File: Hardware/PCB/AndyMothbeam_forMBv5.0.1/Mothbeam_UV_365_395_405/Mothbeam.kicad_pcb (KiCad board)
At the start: 2 copper layers, 27.8 x 45 mm, 23 parts, among them CN1 X6511FRS-04-C85D30, SW2 SW_DIP_x04, U1 BCR421U, U2 BCR421U, U3 BCR421U

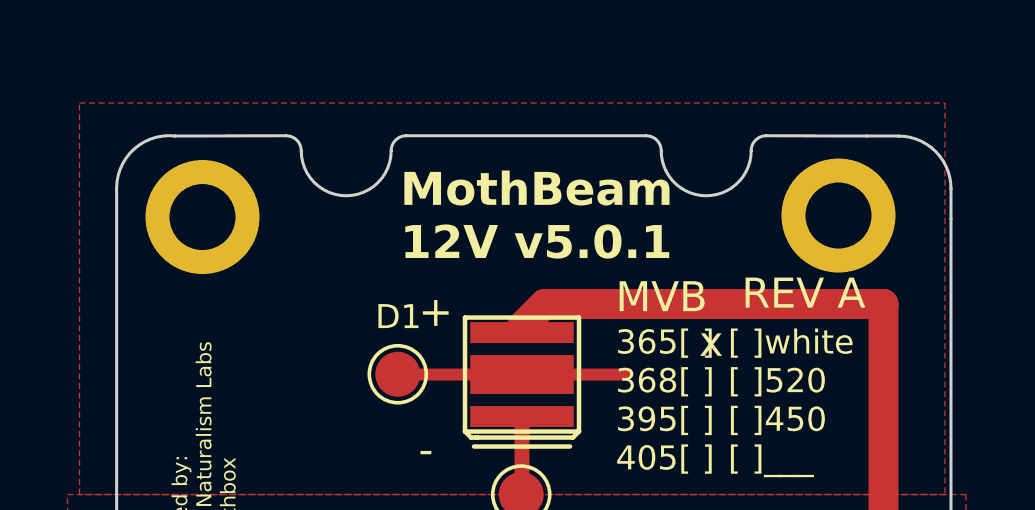
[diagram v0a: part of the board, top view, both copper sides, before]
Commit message: MADE UV m3 holes ready for JLCPCB
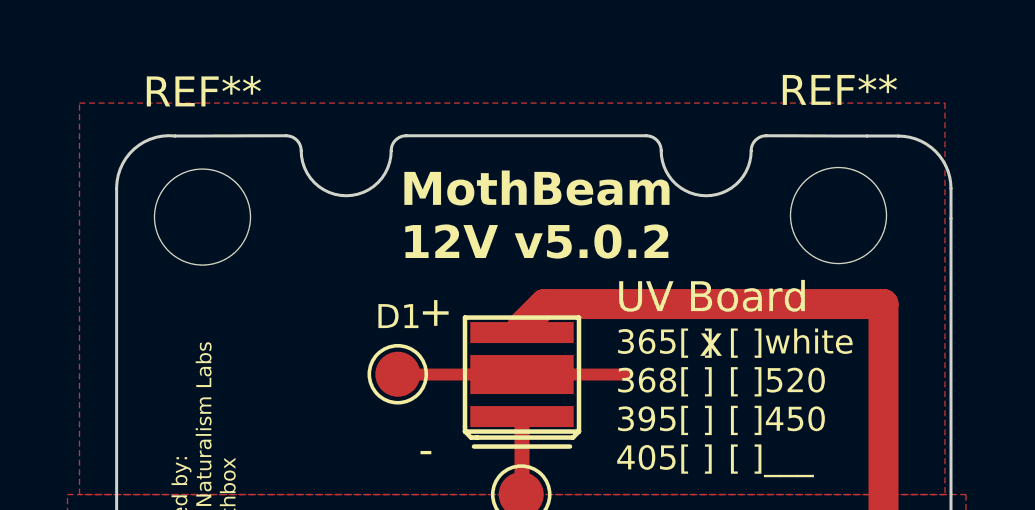
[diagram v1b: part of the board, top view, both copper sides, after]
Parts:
- REF** (x2): value MountingHole_2.2mm_M2_DIN965_Pad -> MountingHole_3.2mm_M3; footprint MountingHole:MountingHole_2.2mm_M2_DIN965_Pad -> MountingHole:MountingHole_3.2mm_M3
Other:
- board text added: "MothBeam 12V v5.0.2"
- board text added: "UV Board"
- board text removed: "MVB"
- board text removed: "MothBeam 12V v5.0.1"
- board text removed: "REV A"
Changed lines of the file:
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@@
 	(net 16 "Net-(D1--)")
 	(net 17 "Net-(D2-A)")
-	(footprint "MountingHole:MountingHole_2.2mm_M2_DIN965_Pad"
+	(footprint "MountingHole:MountingHole_3.2mm_M3"
 		(layer "F.Cu")
 		(at 102.1 32.7)
-		(descr "Mounting Hole 2.2mm, M2, generated by kicad-footprint-generator mountinghole.py")
-		(tags "mountinghole M2 DIN965")
+		(descr "Mounting Hole 3.2mm, M3, no annular, generated by kicad-footprint-generator mountinghole.py")
+		(tags "mountinghole M3")
 		(property "Reference" "REF**"
-			(at 0 -2.85 0)
+			(at 0 -4.15 0)
 			(layer "F.SilkS")
-			(hide yes)
 			(effects
 				(font
-					(size 0.8 0.8)
+					(size 1 1)
 					(thickness 0.15)
 				)
 			)
 		)
-		(property "Value" "MountingHole_2.2mm_M2_DIN965_Pad"
-			(at 0 2.85 0)
+		(property "Value" "MountingHole_3.2mm_M3"
+			(at 0 4.15 0)
 			(layer "F.Fab")
 			(effects
@@
 		(fp_circle
 			(center 0 0)
-			(end 1.9 0)
+			(end 3.2 0)
 			(stroke
 				(width 0.15)
@@
 		(fp_circle
 			(center 0 0)
-			(end 2.15 0)
+			(end 3.45 0)
 			(stroke
 				(width 0.05)
@@
 			(effects
 				(font
-					(size 0.95 0.95)
-					(thickness 0.14)
+					(size 1 1)
+					(thickness 0.15)
 				)
 			)
 		)
-		(pad "1" thru_hole circle
+		(pad "" np_thru_hole circle
 			(at 0 0)
-			(size 3.8 3.8)
-			(drill 2.2)
+			(size 3.2 3.2)
+			(drill 3.2)
 			(layers "*.Cu" "*.Mask")
-			(remove_unused_layers no)
-			(zone_connect 2)
 		)
 		(embedded_fonts no)
@@
 		)
 	)
-	(footprint "MountingHole:MountingHole_2.2mm_M2_DIN965_Pad"
+	(footprint "MountingHole:MountingHole_3.2mm_M3"
 		(layer "F.Cu")
 		(at 123.3 32.65)
-		(descr "Mounting Hole 2.2mm, M2, generated by kicad-footprint-generator mountinghole.py")
-		(tags "mountinghole M2 DIN965")
+		(descr "Mounting Hole 3.2mm, M3, no annular, generated by kicad-footprint-generator mountinghole.py")
+		(tags "mountinghole M3")
 		(property "Reference" "REF**"
-			(at 0 -2.85 0)
+			(at 0 -4.15 0)
 			(layer "F.SilkS")
-			(hide yes)
 			(effects
 				(font
-					(size 0.8 0.8)
+					(size 1 1)
 					(thickness 0.15)
 				)
 			)
 		)
-		(property "Value" "MountingHole_2.2mm_M2_DIN965_Pad"
-			(at 0 2.85 0)
+		(property "Value" "MountingHole_3.2mm_M3"
+			(at 0 4.15 0)
 			(layer "F.Fab")
 			(effects
@@
 		(fp_circle
 			(center 0 0)
-			(end 1.9 0)
+			(end 3.2 0)
 			(stroke
 				(width 0.15)
@@
 		(fp_circle
 			(center 0 0)
-			(end 2.15 0)
+			(end 3.45 0)
 			(stroke
 				(width 0.05)
@@
 			(effects
 				(font
-					(size 0.95 0.95)
-					(thickness 0.14)
+					(size 1 1)
+					(thickness 0.15)
 				)
 			)
 		)
-		(pad "1" thru_hole circle
+		(pad "" np_thru_hole circle
 			(at 0 0)
-			(size 3.8 3.8)
-			(drill 2.2)
+			(size 3.2 3.2)
+			(drill 3.2)
 			(layers "*.Cu" "*.Mask")
-			(remove_unused_layers no)
-			(zone_connect 2)
 		)
 		(embedded_fonts no)
@@
 		)
 	)
-	(gr_text "REV A"
-		(at 120.07 35.84 0)
-		(layer "F.SilkS")
-		(effects
-			(font
-				(size 1 1)
-				(thickness 0.15)
-			)
-			(justify left bottom)
-		)
-	)
 	(gr_text "x"
 		(at 118.55 55.6 0)
@@
 		)
 	)
-	(gr_text "MothBeam\n12V v5.0.1"
+	(gr_text "MothBeam\n12V v5.0.2"
 		(at 108.69 34.2 0)
 		(layer "F.SilkS" knockout)
@@
 			(justify left bottom)
 		)
-		(render_cache "MothBeam\n12V v5.0.1" 0
+		(render_cache "MothBeam\n12V v5.0.2" 0
 			(polygon
 				(pts
@@
 			(polygon
 				(pts
-					(xy 115.999693 34.013) (xy 115.767162 34.013) (xy 115.767162 33.376997) (xy 115.768707 33.27309)
-					(xy 115.773341 33.158302) (xy 115.740228 33.191415) (xy 115.693278 33.23373) (xy 115.566938 33.335421)
-					(xy 115.454568 33.195244) (xy 115.808738 32.913412) (xy 115.999693 32.913412)
+					(xy 116.193738 34.013) (xy 115.425283 34.013) (xy 115.425283 33.851329) (xy 115.700935 33.572587)
+					(xy 115.834933 33.428581) (xy 115.880699 33.370849) (xy 115.908817 33.323868) (xy 115.926106 33.27531)
+					(xy 115.931922 33.222984) (xy 115.927386 33.180351) (xy 115.915048 33.148366) (xy 115.895719 33.12445)
+					(xy 115.86987 33.106988) (xy 115.837855 33.096013) (xy 115.797991 33.092076) (xy 115.736043 33.099294)
+					(xy 115.67474 33.12136) (xy 115.615191 33.155418) (xy 115.548467 33.204513) (xy 115.422193 33.055134)
+					(xy 115.522272 32.9789) (xy 115.579286 32.946623) (xy 115.646262 32.920397) (xy 115.720273 32.904058)
+					(xy 115.814918 32.898031) (xy 115.885918 32.902734) (xy 115.947282 32.916089) (xy 116.000499 32.937323)
+					(xy 116.049213 32.967155) (xy 116.088909 33.002481) (xy 116.120594 33.043581) (xy 116.143986 33.089802)
+					(xy 116.158135 33.14002) (xy 116.162976 33.195244) (xy 116.15883 33.254988) (xy 116.146699 33.310199)
+					(xy 116.126773 33.361616) (xy 116.083716 33.434901) (xy 116.021993 33.510995) (xy 115.949161 33.585977)
+					(xy 115.856494 33.67421) (xy 115.714839 33.806663) (xy 115.714839 33.81741) (xy 116.193738 33.81741)
 				)
 			)
 		)
 	)
-	(gr_text "MVB"
+	(gr_text "UV Board"
 		(at 115.87 35.96 0)
 		(layer "F.SilkS")
@@
 	)
 	(zone
+		(net 9)
+		(net_name "/T2")
+		(layer "F.Cu")
+		(hatch edge 0.5)
+		(connect_pads
+			(clearance 0.35)
+		)
+		(min_thickness 0.25)
+		(filled_areas_thickness no)
+		(fill yes
+			(thermal_gap 0.5)
+			(thermal_bridge_width 0.5)
+			(smoothing chamfer)
+		)
+		(polygon
+			(pts
+				(xy 127.55 41.95) (xy 127.55 49.95) (xy 97.6 49.95) (xy 97.6 41.95)
+			)
+		)
+	)
+	(zone
 		(net 16)
 		(net_name "Net-(D1--)")
@@
 		(name "$teardrop_padvia$")
 		(hatch none 0.1)
-		(priority 30000)
+		(priority 30003)
 		(attr
 			(teardrop
@@
 		(polygon
 			(pts
-				(xy 112.2246 43.435589) (xy 113.2246 43.435589) (xy 113.460189 42.096318) (xy 112.7246 41.949) (xy 111.989011 42.096318)
-			)
-		)
-	)
-	(zone
-		(net 9)
-		(net_name "/T2")
-		(layer "F.Cu")
-		(hatch edge 0.5)
-		(connect_pads
-			(clearance 0.35)
-		)
-		(min_thickness 0.25)
-		(filled_areas_thickness no)
-		(fill yes
-			(thermal_gap 0.5)
-			(thermal_bridge_width 0.5)
-			(smoothing chamfer)
-		)
-		(polygon
-			(pts
-				(xy 127.55 41.95) (xy 127.55 49.95) (xy 97.6 49.95) (xy 97.6 41.95)
+				(xy 113 40.464411) (xy 112.5 40.464411) (xy 111.989011 41.803682) (xy 112.7246 41.951) (xy 113.460189 41.803682)
 			)
 		)
@@
 		(name "$teardrop_padvia$")
 		(hatch none 0.1)
-		(priority 30002)
+		(priority 30001)
 		(attr
 			(teardrop
@@
 		(polygon
 			(pts
-				(xy 112.25 51.435589) (xy 113.25 51.435589) (xy 113.485589 50.096318) (xy 112.75 49.949) (xy 112.014411 50.096318)
+				(xy 113.25 48.464411) (xy 112.25 48.464411) (xy 112.014411 49.803682) (xy 112.75 49.951) (xy 113.485589 49.803682)
 			)
 		)
 	)
 	(zone
-		(net 16)
-		(net_name "Net-(D1--)")
+		(net 17)
+		(net_name "Net-(D2-A)")
 		(layer "F.Cu")
 		(name "$teardrop_padvia$")
 		(hatch none 0.1)
-		(priority 30003)
+		(priority 30002)
 		(attr
 			(teardrop
@@
 		(polygon
 			(pts
-				(xy 113 40.464411) (xy 112.5 40.464411) (xy 111.989011 41.803682) (xy 112.7246 41.951) (xy 113.460189 41.803682)
+				(xy 112.25 51.435589) (xy 113.25 51.435589) (xy 113.485589 50.096318) (xy 112.75 49.949) (xy 112.014411 50.096318)
 			)
 		)
@@
 	)
 	(zone
-		(net 17)
-		(net_name "Net-(D2-A)")
+		(net 16)
+		(net_name "Net-(D1--)")
 		(layer "F.Cu")
 		(name "$teardrop_padvia$")
 		(hatch none 0.1)
-		(priority 30001)
+		(priority 30000)
 		(attr
 			(teardrop
@@
 		(polygon
 			(pts
-				(xy 113.25 48.464411) (xy 112.25 48.464411) (xy 112.014411 49.803682) (xy 112.75 49.951) (xy 113.485589 49.803682)
+				(xy 112.2246 43.435589) (xy 113.2246 43.435589) (xy 113.460189 42.096318) (xy 112.7246 41.949) (xy 111.989011 42.096318)
 			)
 		)
